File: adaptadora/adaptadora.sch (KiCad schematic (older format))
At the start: 39 parts, among them J1 Conn_Coaxial, J10 Conn_01x02, J11 Conn_Coaxial, J12 Conn_Coaxial, J2 Conn_Coaxial, J3 Conn_Coaxial, J4 Conn_Coaxial, J5 Conn_Coaxial, J6 Conn_01x02, J7 Conn_02x20_Odd_Even, J8 Conn_02x20_Odd_Even, J9 Conn_01x04, U1 LM361MX_NOPB-LM361MX_NOPB, U2 TLV2772IDR

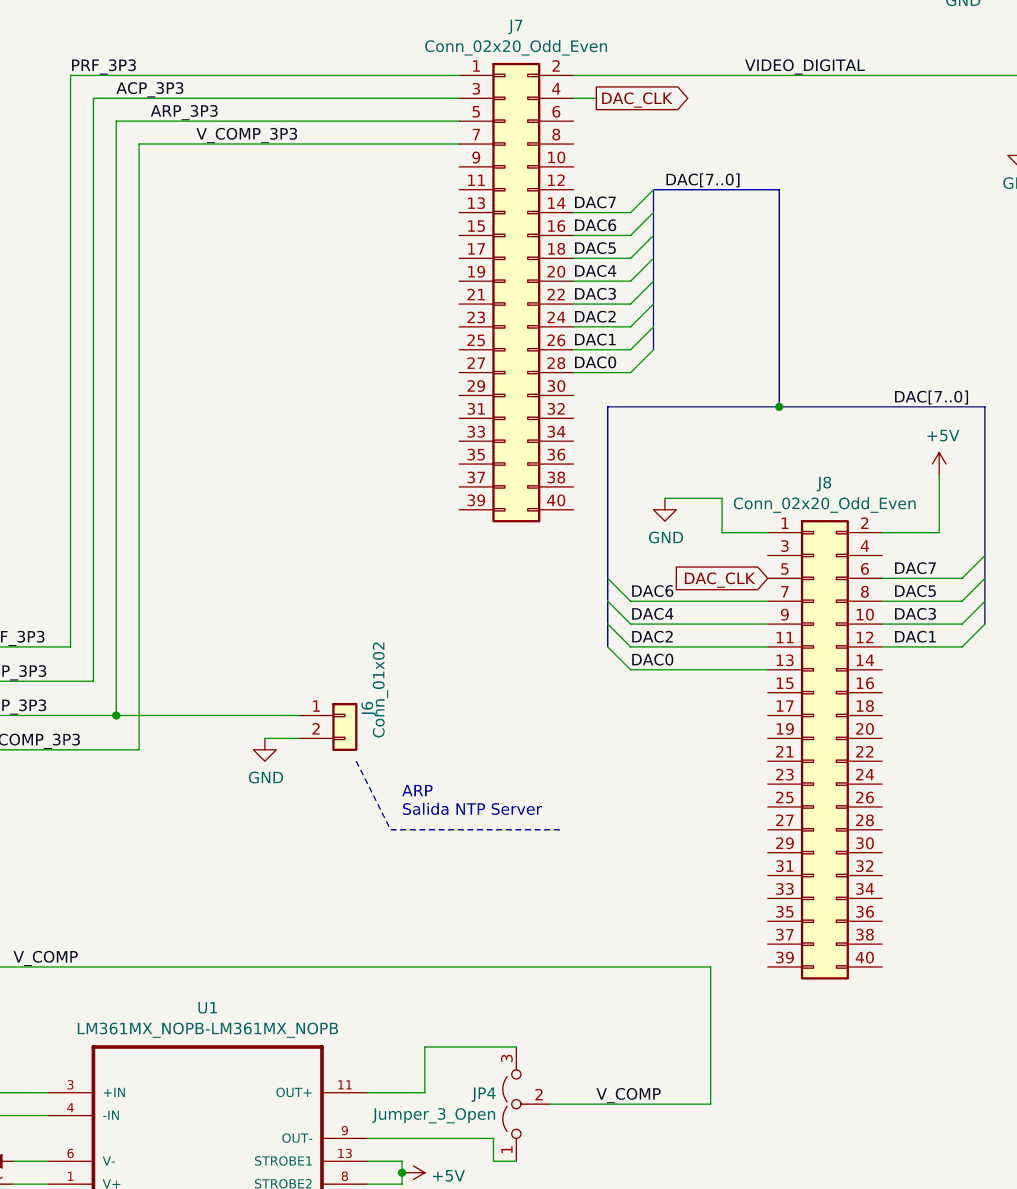
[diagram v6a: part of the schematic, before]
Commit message: se agrega texto
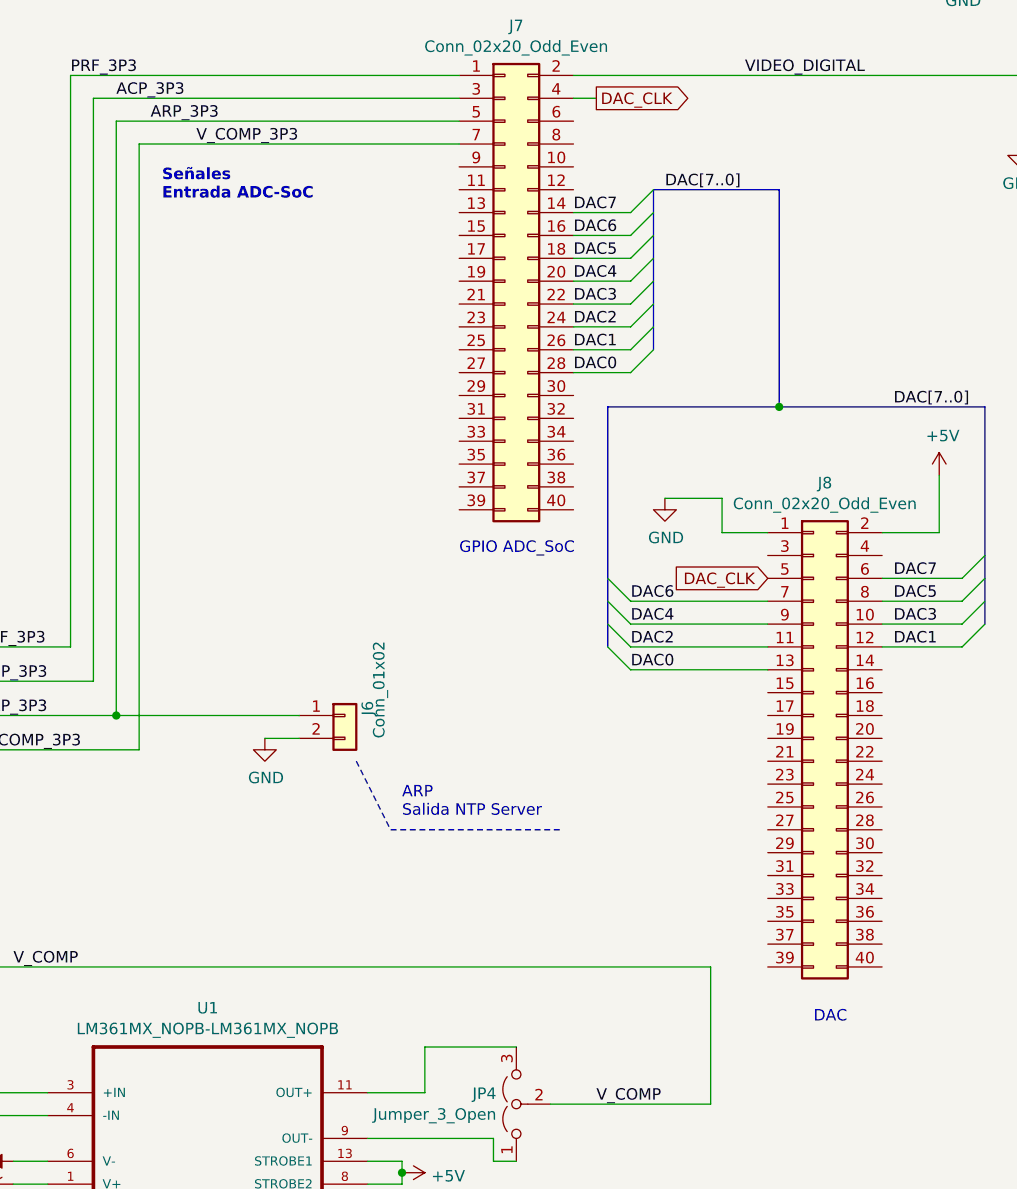
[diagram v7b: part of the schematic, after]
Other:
- note added: "DAC"
- note added: "GPIO ADC_SoC"
- note added: "Señales\nEntrada ADC-SoC"
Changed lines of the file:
@@
 Wire Bus Line
 	6500 2400 6500 3100
+Text Notes 4350 2450 0    50   ~ 10
+Señales\nEntrada ADC-SoC
+Text Notes 5650 4000 0    50   ~ 0
+GPIO ADC_SoC
+Text Notes 7200 6050 0    50   ~ 0
+DAC
 $EndSCHEMATC
